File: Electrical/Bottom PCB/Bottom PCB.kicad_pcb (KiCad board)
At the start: 2 copper layers, 100 x 80 mm, 66 parts, among them J101 Steper1, J102 Steper2, J201 PROGRAMMING, J202 MainIO, J301 Battery, Q201 BC847, Q202 BC847, SW101 FL, SW102 FR, SW301 SW_SPST, U101 QRE1113, U102 ULN2003A, U103 MCP23017_SO, U104 QRE1113, U105 QRE1113, U106 QRE1113, U201 ESP32-WROVER, U301 MC78M05_TO252

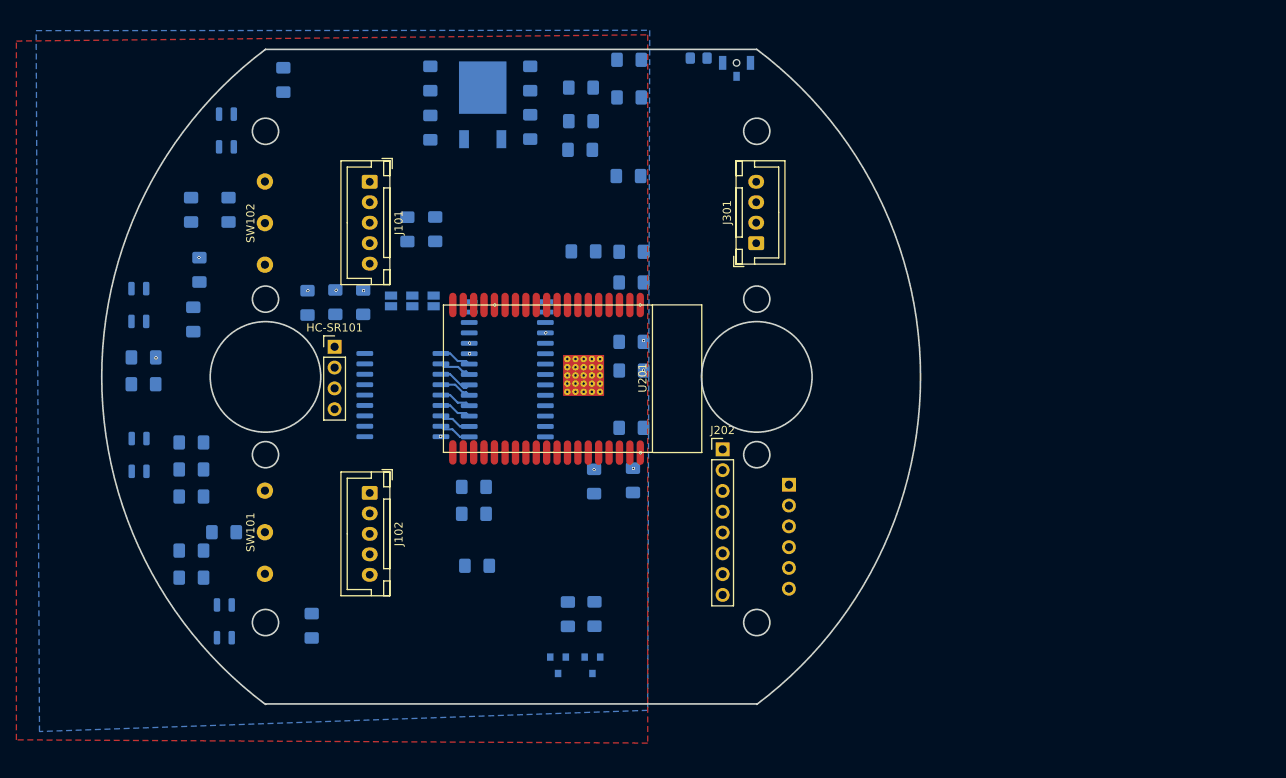
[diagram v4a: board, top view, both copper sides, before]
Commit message: changed from 1206 to 0805
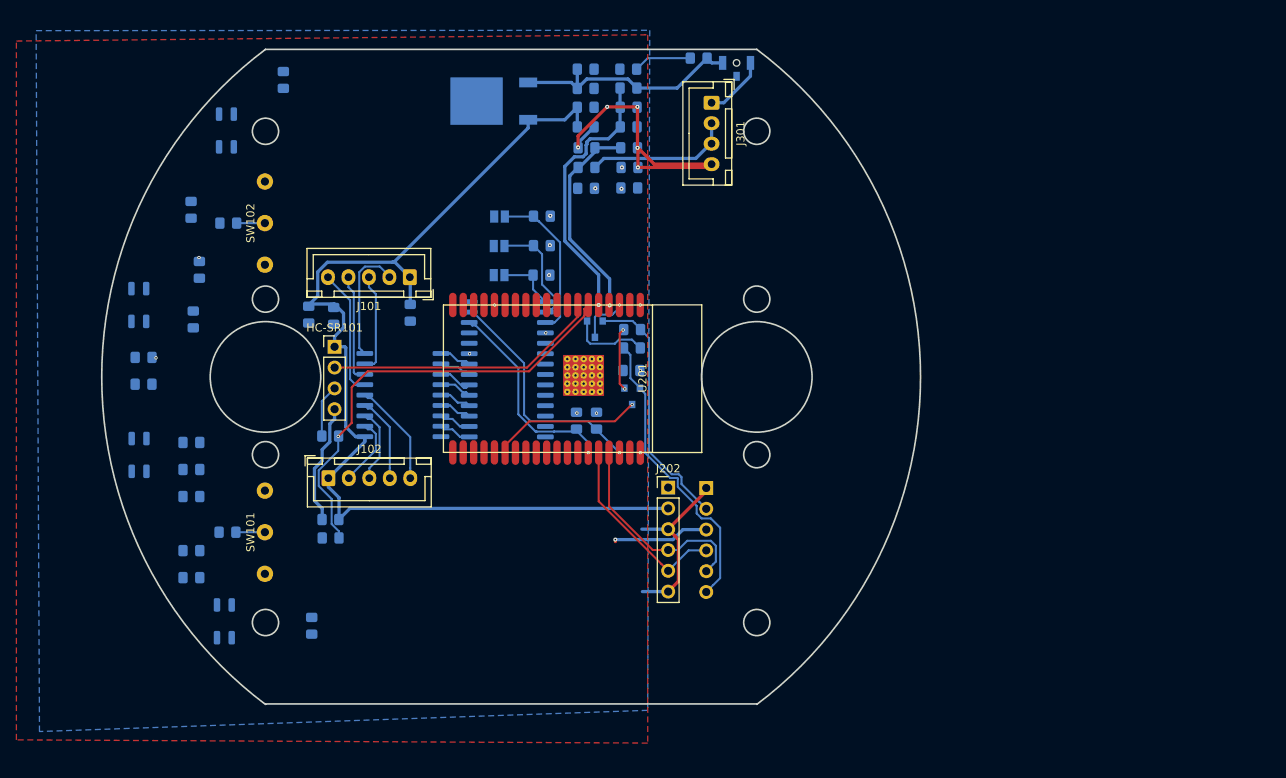
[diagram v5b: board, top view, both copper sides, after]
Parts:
- C101, C102, C103, C104, C105, C106, C107, C108, C201, C202, C203, C204, C301, C302, C303, C304, C305, C306: footprint Capacitor_SMD:C_1206_3216Metric_Pad1.42x1.75mm_HandSolder -> Capacitor_SMD:C_0805_2012Metric_Pad1.15x1.40mm_HandSolder
- J202: footprint Connector_PinHeader_2.54mm:PinHeader_1x08_P2.54mm_Vertical -> Connector_PinHeader_2.54mm:PinHeader_1x06_P2.54mm_Vertical
- R101, R102, R103, R104, R105, R106, R107, R108, R109, R110, R111, R112, R113, R114, R115, R201, R202, R203, R204, R301, R302, R303, R304, R305: footprint Resistor_SMD:R_1206_3216Metric_Pad1.42x1.75mm_HandSolder -> Resistor_SMD:R_0805_2012Metric_Pad1.15x1.40mm_HandSolder
- moved Q201 41.1 mm to (159.3, 83.7)
- moved R204 35.6 mm to (163.8, 83.8), turned to 180 degrees
- moved Q202 34.1 mm to (163.8, 91.9)
- moved R203 32.8 mm to (163.8, 86.0), turned to 0 degrees
- moved R109 30.5 mm to (152.8, 69.9), turned to 0 degrees
- moved C105 30.4 mm to (136.8, 81.7), turned to 270 degrees
- moved R110 26.2 mm to (152.8, 73.5), turned to 0 degrees
- moved R111 22.0 mm to (152.8, 77.1), turned to 0 degrees
- moved R102 20.0 mm to (127.0, 96.8), turned to 180 degrees
- moved C304 19.9 mm to (158.2, 59.0), turned to 0 degrees
- moved C203 19.5 mm to (158.2, 66.5)
- moved C303 19.1 mm to (158.2, 56.6), turned to 0 degrees
- moved C102 18.8 mm to (127.0, 107.0)
- moved R103 18.6 mm to (127.0, 109.2), turned to 180 degrees
- moved J301 18.0 mm to (173.6, 56.0), turned to 270 degrees
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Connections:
- net Net-(J301-Pad1) renamed /Bat Managment/PowerIn
- HC-SR101 pad 2: (no net) -> Sonar_Trig
- J202 pad 1: GND -> (no net)
- J202 pad 2: (no net) -> +5V
- J202 pad 3: (no net) -> GND
- J202 pad 4: +5V -> TX
- J202 pad 5: GND -> RX
- J202 pad 6: TX -> GND
- U102 pad 11: Net-(J102-Pad5) -> Net-(J102-Pad2)
- U102 pad 12: Net-(J102-Pad4) -> Net-(J102-Pad3)
- U102 pad 13: Net-(J102-Pad3) -> Net-(J102-Pad4)
- U102 pad 14: Net-(J102-Pad2) -> Net-(J102-Pad5)
- U201 pad 4: BatV -> half_BatV
- U201 pad 5: half_BatV -> BatV
- U201 pad 6: (no net) -> Sonar_Echo
- U201 pad 7: (no net) -> Sonar_Trig
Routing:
- net +5V: track 0.00 -> 130.3 mm
- net GND: track 0.00 -> 77.0 mm, vias 5 -> 8
- net Sonar_Echo: track 0.00 -> 54.8 mm, vias 0 -> 1
- net /ESP32-WROVER/DTR: track 0.00 -> 36.6 mm
- net Sonar_Trig: track 0.00 -> 33.7 mm
- net BatV: track 0.00 -> 33.0 mm, vias 0 -> 1
- net /ESP32-WROVER/CTS: track 0.00 -> 30.6 mm
- net SDA: track 0.00 -> 29.2 mm, vias 0 -> 1
- net +BATT: track 0.00 -> 29.1 mm
- net TX: track 0.00 -> 26.1 mm
- net half_BatV: track 0.00 -> 25.8 mm, vias 0 -> 1
- net SCL: track 0.00 -> 25.2 mm, vias 0 -> 1
- net RX: track 0.00 -> 23.6 mm
- net Net-(JP101-Pad1): track 0.00 -> 19.2 mm
- net GPIO0: track 0.00 -> 18.5 mm, vias 0 -> 1
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
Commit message: hello
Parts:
- removed C101, C102, C104, C106, C107, C108, C203, C204: 100pF, Capacitor_SMD:C_0805_2012Metric_Pad1.15x1.40mm_HandSolder
- removed C103, C105, C201, C202, C306: 10uF, Capacitor_SMD:C_0805_2012Metric_Pad1.15x1.40mm_HandSolder
- removed HC-SR101: HC-SR04, Connector_PinHeader_2.54mm:PinHeader_1x04_P2.54mm_Vertical
- removed J101: Steper1, Connector_JST:JST_XH_B5B-XH-A_1x05_P2.50mm_Vertical
- removed J102: Steper2, Connector_JST:JST_XH_B5B-XH-A_1x05_P2.50mm_Vertical
- removed J201: PROGRAMMING, Connector_PinHeader_2.54mm:PinHeader_1x06_P2.54mm_Vertical
- removed J202: MainIO, Connector_PinHeader_2.54mm:PinHeader_1x06_P2.54mm_Vertical
- removed JP101: A2, Jumper:SolderJumper-2_P1.3mm_Open_Pad1.0x1.5mm
- removed JP102: A1, Jumper:SolderJumper-2_P1.3mm_Open_Pad1.0x1.5mm
- removed JP103: A0, Jumper:SolderJumper-2_P1.3mm_Open_Pad1.0x1.5mm
- removed Q201, Q202: BC847, Package_TO_SOT_SMD:SOT-23
- removed R101, R104, R106, R108, R113, R115: 10k, Resistor_SMD:R_0805_2012Metric_Pad1.15x1.40mm_HandSolder
- removed R102: 2k7, Resistor_SMD:R_0805_2012Metric_Pad1.15x1.40mm_HandSolder
- removed R103: 4k7, Resistor_SMD:R_0805_2012Metric_Pad1.15x1.40mm_HandSolder
- removed R105, R107, R112, R114: 100, Resistor_SMD:R_0805_2012Metric_Pad1.15x1.40mm_HandSolder
- removed R109, R110, R111: 47k, Resistor_SMD:R_0805_2012Metric_Pad1.15x1.40mm_HandSolder
- removed R203, R204: 10K, Resistor_SMD:R_0805_2012Metric_Pad1.15x1.40mm_HandSolder
- removed the R304 at (163.5, 61.5)
- removed SW101: FL, DF-M Series Micro Switches:TypeD
- removed SW102: FR, DF-M Series Micro Switches:TypeC
- removed U101, U104, U105, U106: QRE1113, OptoDevice:OnSemi_CASE100CY
- removed U102: ULN2003A, Package_SO:SOIC-18W_7.5x11.6mm_P1.27mm
- removed U103: MCP23017_SO, Package_SO:SOIC-28W_7.5x17.9mm_P1.27mm
- added D201: LED, LED_SMD:LED_0805_2012Metric_Pad1.15x1.40mm_HandSolder, B.Cu at (195.5, 82.0)
- added D301: SS24, Diode_SMD:D_SMB-SMC_Universal_Handsoldering, B.Cu at (181.0, 111.6)
- added D303: SS24, Diode_SMD:D_SMB-SMC_Universal_Handsoldering, B.Cu at (181.0, 104.5)
- added D304: SS24, Diode_SMD:D_SMB-SMC_Universal_Handsoldering, B.Cu at (236.3, 91.7)
- added D305: Charging, LED_SMD:LED_0805_2012Metric_Pad1.15x1.40mm_HandSolder, B.Cu at (195.5, 89.5)
- added D306: Standby, LED_SMD:LED_0805_2012Metric_Pad1.15x1.40mm_HandSolder, B.Cu at (195.5, 96.5)
- added D307: SS24, Diode_SMD:D_SMB-SMC_Universal_Handsoldering, B.Cu at (211.8, 99.8)
- added D308: SS24, Diode_SMD:D_SMB-SMC_Universal_Handsoldering, F.Cu at (107.7, 69.7)
- added D309: SS24, Diode_SMD:D_SMB-SMC_Universal_Handsoldering, B.Cu at (224.0, 99.8)
- added D310: SS24, Diode_SMD:D_SMB-SMC_Universal_Handsoldering, B.Cu at (224.0, 92.0)
- added D311: SS24, Diode_SMD:D_SMB-SMC_Universal_Handsoldering, F.Cu at (120.0, 69.7)
- added H301: +VE, TestPoint:TestPoint_Pad_D2.0mm, F.Cu at (103.6, 75.6)
- added H302: -Ve, TestPoint:TestPoint_Pad_D2.0mm, F.Cu at (107.7, 75.6)
- added HC-SR501: HC-SR04, Connector_PinHeader_2.54mm:PinHeader_1x04_P2.54mm_Vertical, F.Cu at (127.0, 65.4)
- added J401: Steper1, Connector_JST:JST_XH_B5B-XH-A_1x05_P2.50mm_Vertical, F.Cu at (132.5, 102.5)
- added J402: Steper2, Connector_JST:JST_XH_B5B-XH-A_1x05_P2.50mm_Vertical, F.Cu at (142.5, 78.5)
- added R305: 30k, Resistor_SMD:R_0603_1608Metric_Pad0.98x0.95mm_HandSolder, B.Cu at (177.9, 72.3)
- added R306: 10k, Resistor_SMD:R_0603_1608Metric_Pad0.98x0.95mm_HandSolder, B.Cu at (172.9, 67.3)
- added R307: 2R, Resistor_SMD:R_0603_1608Metric_Pad0.98x0.95mm_HandSolder, B.Cu at (199.0, 107.0)
- added R308: 2R, Resistor_SMD:R_0603_1608Metric_Pad0.98x0.95mm_HandSolder, B.Cu at (204.9, 108.0)
- added R309: 1k, Resistor_SMD:R_0603_1608Metric_Pad0.98x0.95mm_HandSolder, B.Cu at (215.0, 116.7)
- added R310: 1k, Resistor_SMD:R_0603_1608Metric_Pad0.98x0.95mm_HandSolder, B.Cu at (215.0, 114.2)
- added R311: 1k2, Resistor_SMD:R_0603_1608Metric_Pad0.98x0.95mm_HandSolder, B.Cu at (219.4, 116.7)
- added R501: 10k, Resistor_SMD:R_0603_1608Metric_Pad0.98x0.95mm_HandSolder, B.Cu at (123.0, 109.9)
- added R503: 10k, Resistor_SMD:R_0603_1608Metric_Pad0.98x0.95mm_HandSolder, B.Cu at (123.0, 70.4)
- added R505: 100, Resistor_SMD:R_0603_1608Metric_Pad0.98x0.95mm_HandSolder, B.Cu at (115.5, 54.9)
- added R506: 10k, Resistor_SMD:R_0603_1608Metric_Pad0.98x0.95mm_HandSolder, B.Cu at (127.5, 51.4)
- added R507: 100, Resistor_SMD:R_0603_1608Metric_Pad0.98x0.95mm_HandSolder, B.Cu at (103.4, 74.5)
- added R508: 10k, Resistor_SMD:R_0603_1608Metric_Pad0.98x0.95mm_HandSolder, B.Cu at (107.4, 84.5)
- added R509: 100, Resistor_SMD:R_0603_1608Metric_Pad0.98x0.95mm_HandSolder, B.Cu at (103.4, 84.5)
- added R510: 10k, Resistor_SMD:R_0603_1608Metric_Pad0.98x0.95mm_HandSolder, B.Cu at (107.4, 94.5)
- added R511: 100, Resistor_SMD:R_0603_1608Metric_Pad0.98x0.95mm_HandSolder, B.Cu at (103.4, 94.6)
- added R512: 10k, Resistor_SMD:R_0603_1608Metric_Pad0.98x0.95mm_HandSolder, B.Cu at (107.4, 104.5)
- added R513: 2k7, Resistor_SMD:R_0603_1608Metric_Pad0.98x0.95mm_HandSolder, B.Cu at (131.0, 70.0)
- added R514: 4k7, Resistor_SMD:R_0603_1608Metric_Pad0.98x0.95mm_HandSolder, B.Cu at (124.4, 115.0)
- added R515: 100, Resistor_SMD:R_0603_1608Metric_Pad0.98x0.95mm_HandSolder, B.Cu at (115.4, 124.0)
- added R516: 10k, Resistor_SMD:R_0603_1608Metric_Pad0.98x0.95mm_HandSolder, B.Cu at (127.0, 127.6)
- added SW501: FL, DF-M:TypeD, F.Cu at (119.0, 109.0)
- added SW503: FR, DF-M:TypeC, F.Cu at (119.0, 69.5)
- added SWD201: Tag-Connect SWD, Connector:Tag-Connect_TC2030-IDC-NL_2x03_P1.27mm_Vertical, B.Cu at (159.4, 89.7)
- added U202: ATSAMD21G18A-AUT, Package_QFP:TQFP-48_7x7mm_P0.5mm, F.Cu at (151.5, 90.0)
- added U302: AP2112K-3.3, Package_TO_SOT_SMD:SOT-23-5, F.Cu at (172.0, 57.5)
- added U303: TP4056, Package_SO:SOP-8-1EP_4.57x4.57mm_P1.27mm_EP4.57x4.45mm_ThermalVias, F.Cu at (156.7, 103.4)
- added U401: ULN2003A, Package_SO:SOIC-18W_7.5x11.6mm_P1.27mm, F.Cu at (137.5, 90.5)
- added U501: QRE1113, OptoDevice:OnSemi_CASE100AQ, B.Cu at (120.0, 50.5)
- added U502: QRE1113, OptoDevice:OnSemi_CASE100AQ, B.Cu at (102.5, 78.5)
- added U503: QRE1113, OptoDevice:OnSemi_CASE100AQ, B.Cu at (102.5, 89.0)
- added U504: QRE1113, OptoDevice:OnSemi_CASE100AQ, B.Cu at (102.5, 98.5)
- added U505: QRE1113, OptoDevice:OnSemi_CASE100AQ, B.Cu at (119.5, 126.5)
- C301, C304: value 100pF -> 22uF
- C302, C303: value 10uF -> 22uF
- J301: value Battery -> Battery 1S2P
- R201: value 4K7 -> 10k; footprint Resistor_SMD:R_0805_2012Metric_Pad1.15x1.40mm_HandSolder -> Resistor_SMD:R_0603_1608Metric_Pad0.98x0.95mm_HandSolder
- R202: value 4k7 -> 1k; footprint Resistor_SMD:R_0805_2012Metric_Pad1.15x1.40mm_HandSolder -> Resistor_SMD:R_0603_1608Metric_Pad0.98x0.95mm_HandSolder
- R301, R303: footprint Resistor_SMD:R_0805_2012Metric_Pad1.15x1.40mm_HandSolder -> Resistor_SMD:R_0603_1608Metric_Pad0.98x0.95mm_HandSolder
- R302: value 47k -> 73k; footprint Resistor_SMD:R_0805_2012Metric_Pad1.15x1.40mm_HandSolder -> Resistor_SMD:R_0603_1608Metric_Pad0.98x0.95mm_HandSolder
- R304: renamed from R305; footprint Resistor_SMD:R_0805_2012Metric_Pad1.15x1.40mm_HandSolder -> Resistor_SMD:R_0603_1608Metric_Pad0.98x0.95mm_HandSolder
- U201: value ESP32-WROVER -> GD25Q64C; footprint esp32-wrover:ESP32-WROVER -> Package_SO:SOIC-8_5.23x5.23mm_P1.27mm
- U301: value MC78M05_TO252 -> FP6298; footprint Package_TO_SOT_SMD:TO-252-2 -> Package_SO:SOIC-8_3.9x4.9mm_P1.27mm
- moved Logo101 41.8 mm to (190.0, 72.0)
- moved R202 34.6 mm to (189.5, 83.0), turned to 180 degrees
- moved J301 31.5 mm to (164.4, 86.2)
- moved U301 30.0 mm to (171.3, 73.5), turned to 0 degrees
- moved R201 24.6 mm to (156.5, 70.5), turned to 0 degrees
- moved R302 22.6 mm to (177.9, 75.2)
- moved U201 14.1 mm to (161.0, 76.5), turned to 0 degrees
- renumbered D301 to D302
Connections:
- C305 pad 1: BatV -> A0
- J301 pad 1: /Bat Managment/PowerIn -> GND
- J301 pad 2: half_Bat -> GND
- J301 pad 3: half_Bat -> PowerIn
- J301 pad 4: GND -> PowerIn
- R201 pad 2: SDA -> FLASH_CS
- R202 pad 1: +3V3 -> Net-(D201-Pad2)
- R202 pad 2: SCL -> D13
- R301 pad 1: BatV -> A0
- R302 pad 1: half_BatV -> Net-(R302-Pad1)
- R302 pad 2: half_Bat -> +5V
- R303 pad 2: BatV -> A0
- SW301 pad 1: /Bat Managment/PowerIn -> Net-(D309-Pad1)
- U201 pad 1: GND -> FLASH_CS
- U201 pad 2: +3V3 -> FLASH_MISO
- U201 pad 3: EN -> +3V3
- U201 pad 4: half_BatV -> GND
- U201 pad 5: BatV -> FLASH_MOSI
- U201 pad 6: Sonar_Echo -> FLASH_SCK
- U201 pad 7: Sonar_Trig -> +3V3
- U201 pad 8: (no net) -> +3V3
- U301 pad 1: +BATT -> GND
- U301 pad 2: GND -> (no net)
- U301 pad 3: +5V -> +BATT
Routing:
- net A4: track 0.00 -> 79.3 mm, vias 0 -> 1
- net IR: track 0.00 -> 76.5 mm
- net GND: track 77.0 -> 0.88 mm, vias 8 -> 1
- net +5V: track 130.3 -> 62.3 mm, vias 0 -> 2
- net Switches: track 0.00 -> 56.1 mm
- net Sonar_Echo: track 54.8 -> 0.00 mm, vias 1 -> 0
- net A5: track 0.00 -> 50.4 mm, vias 0 -> 1
- net /ESP32-WROVER/DTR: track 36.6 -> 0.00 mm
- net Sonar_Trig: track 33.7 -> 0.00 mm
- net BatV: track 33.0 -> 0.00 mm, vias 1 -> 0
- net /ESP32-WROVER/CTS: track 30.6 -> 0.00 mm
- net SDA: track 29.2 -> 0.00 mm, vias 1 -> 0
- net +BATT: track 29.1 -> 0.00 mm
- net TX: track 26.1 -> 0.00 mm
- net half_BatV: track 25.8 -> 0.00 mm, vias 1 -> 0
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- added copper zone on B.Cu, net +3V3
- added copper zone on F.Cu, net GND
- removed copper zone on F.Cu, net +3V3
- removed copper zone on B.Cu, net GND
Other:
- outline, holes or cut-outs redrawn
- net class Big Power removed
- net class Data removed
- net class Default: clearance 0.2 -> 0.1; trace_width 0.25 -> 0.15; via_dia 0.4 -> 0.6; via_drill 0.2 -> 0.4
- net class Power: clearance 0.2 -> 0.1; via_dia 0.5 -> 0.7; via_drill 0.2 -> 0.5
- rule trace_clearance: 0.2 -> 0.1
- board text added: "SwarmBot copyright Philip McGaw 2021"
- board text removed: "SwarmBot copyright Philip McGaw 2020"
